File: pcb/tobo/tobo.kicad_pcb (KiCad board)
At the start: 2 copper layers, 57.5 x 61 mm, 88 parts, among them J1 Molex 538-54548-2272, J2 Conn_01x02_Pin, J4 Molex 538-54548-2472, J5 Conn_01x09_Pin, J6 Conn_01x09_Pin, J7 Conn_01x09_Pin, J8 Hroparts Elec TYPE-C-31-M-12, U1 TS5A23167, U10 5015, U11 5015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

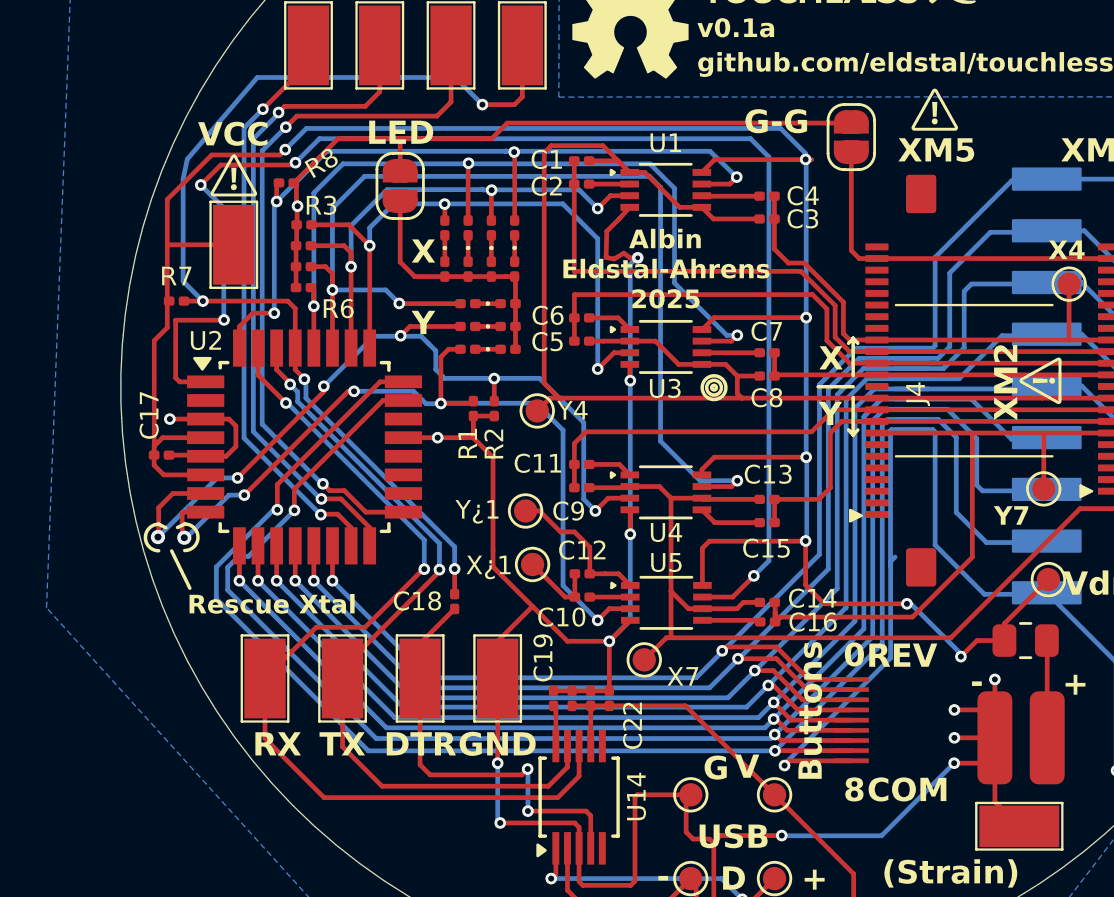
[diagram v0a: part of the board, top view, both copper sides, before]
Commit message: Part numbers selected
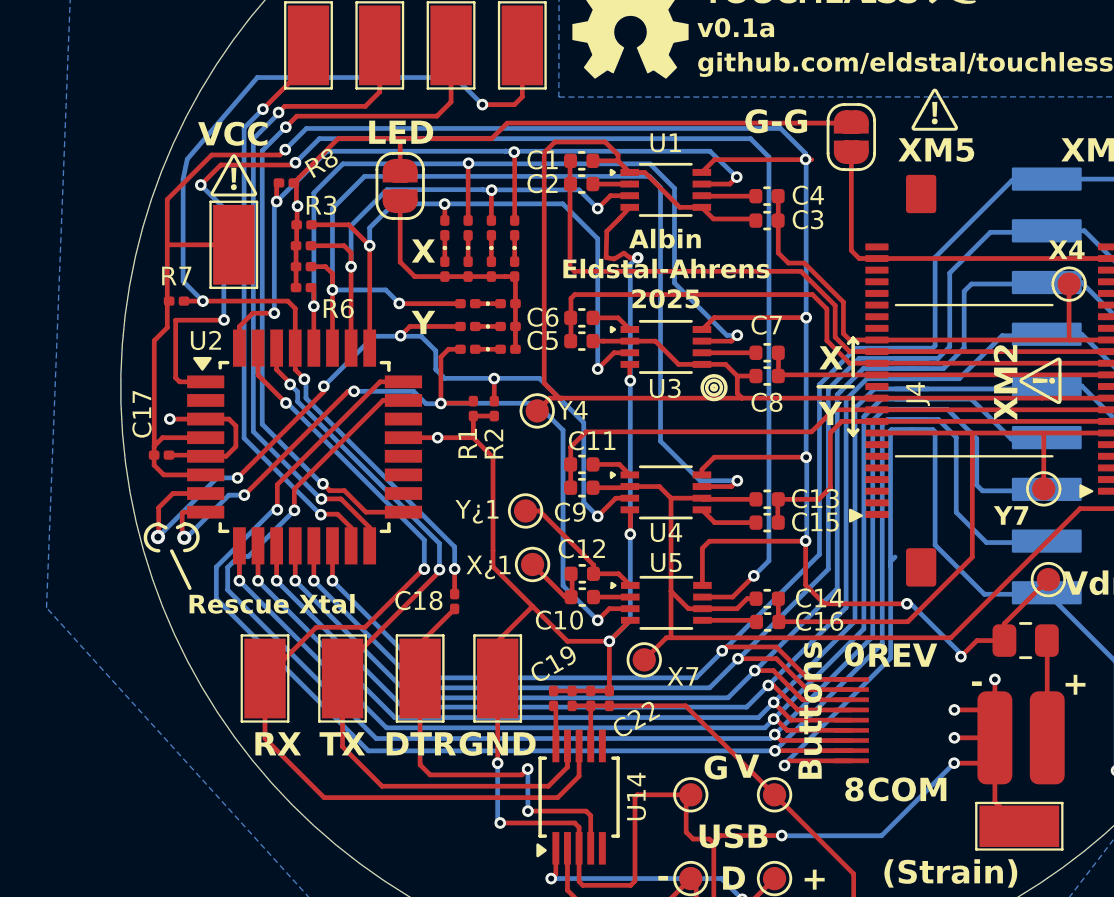
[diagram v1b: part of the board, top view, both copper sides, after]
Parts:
- C1, C10, C11, C12, C13, C14, C15, C16, C2, C3, C4, C5, C6, C7, C8, C9: footprint Capacitor_SMD:C_0201_0603Metric -> Capacitor_SMD:C_0402_1005Metric
- C18: value 100nF -> 0.1uF
- moved C14 0.16 mm to (142.3, 99.1)
- moved C3 0.07 mm to (142.3, 82.8)

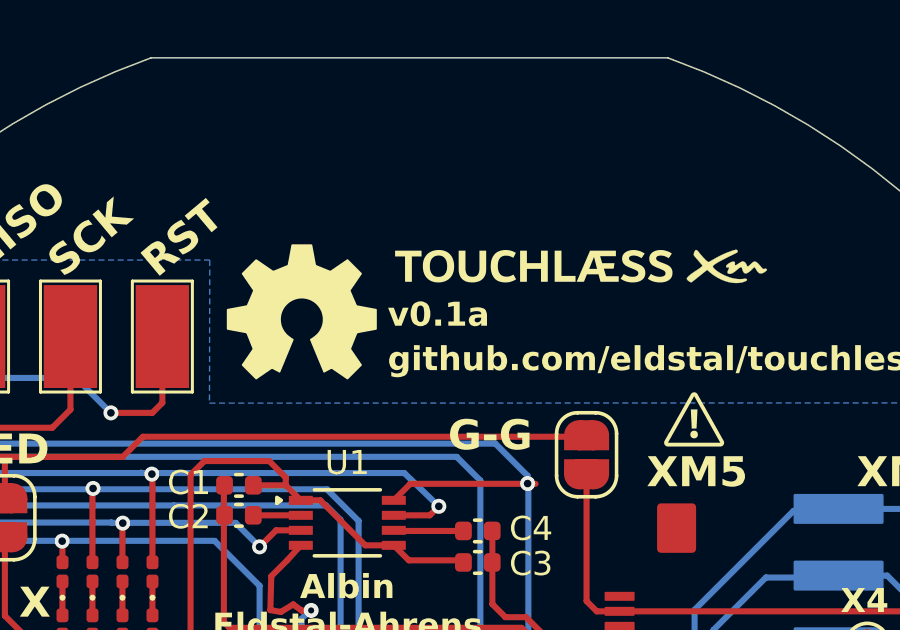
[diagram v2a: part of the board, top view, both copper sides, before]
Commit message: Bumped PCB version to v1.0a
Changes will still be made, I just want it to be labeled
differently from the ones I've ordered for fabrication
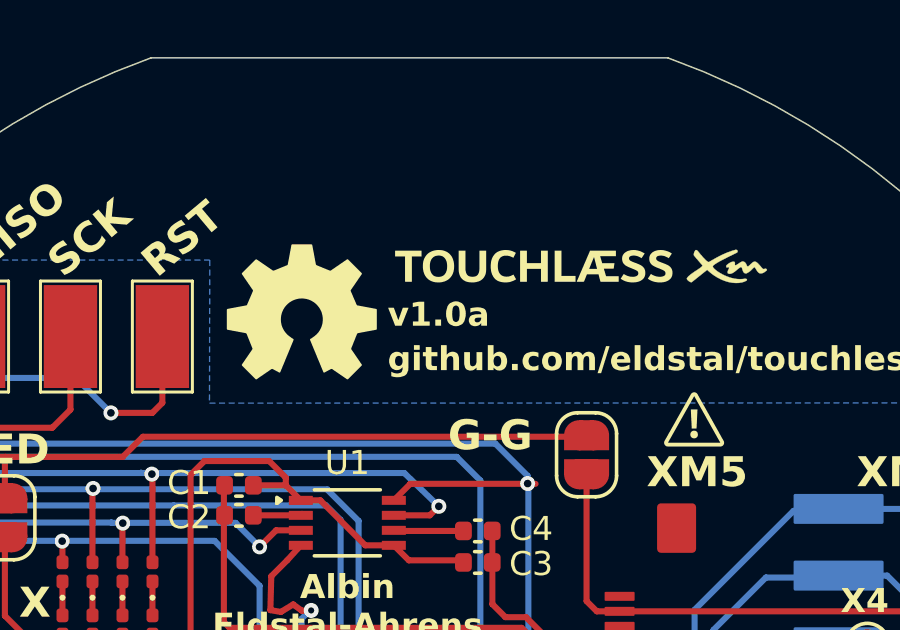
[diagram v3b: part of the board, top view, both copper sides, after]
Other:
- board text added: "v1.0a"
- board text removed: "v0.1a"
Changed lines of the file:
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@@
 		(fp_line
 			(start -2.25 -1.65)
-			(end -2.250001 0.5)
+			(end -2.250002 0.5)
 			(stroke
 				(width 0.1)
@@
 		)
 		(fp_line
-			(start 1.325 -2.099999)
-			(end 1.325 -2.099999)
+			(start 1.325 -2.099998)
+			(end 1.325 -2.099998)
 			(stroke
 				(width 0.2)
@@
 			(start 1.125 -2.1)
 			(mid 1.225001 -2.2)
-			(end 1.325 -2.099999)
+			(end 1.325 -2.099998)
 			(stroke
 				(width 0.2)
@@
 		)
 		(fp_arc
-			(start 1.325 -2.099999)
+			(start 1.325 -2.099998)
 			(mid 1.225 -2.000001)
 			(end 1.125 -2.1)
@@
 		)
 	)
-	(gr_text "v0.1a"
+	(gr_text "v1.0a"
 		(at 139.267504 75.028047 0)
 		(layer "F.SilkS")

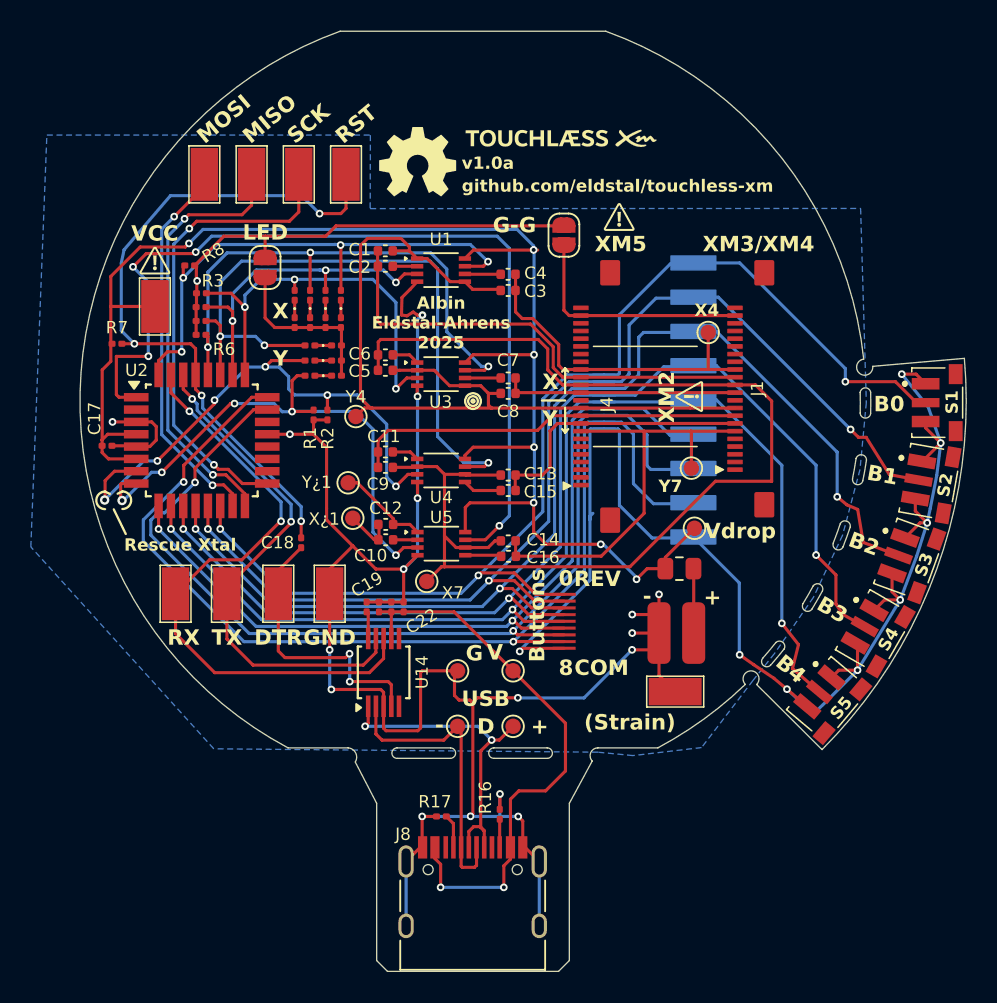
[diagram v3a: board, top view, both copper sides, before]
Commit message: Made the board significantly cheaper to manufacture.
Now there's only one connector (these things are like $5 each :D)
and some of the caps were super expensive too.

Also fixed some incomplete part numbers, so the BOM should be
better for the next attempt at fabrication.
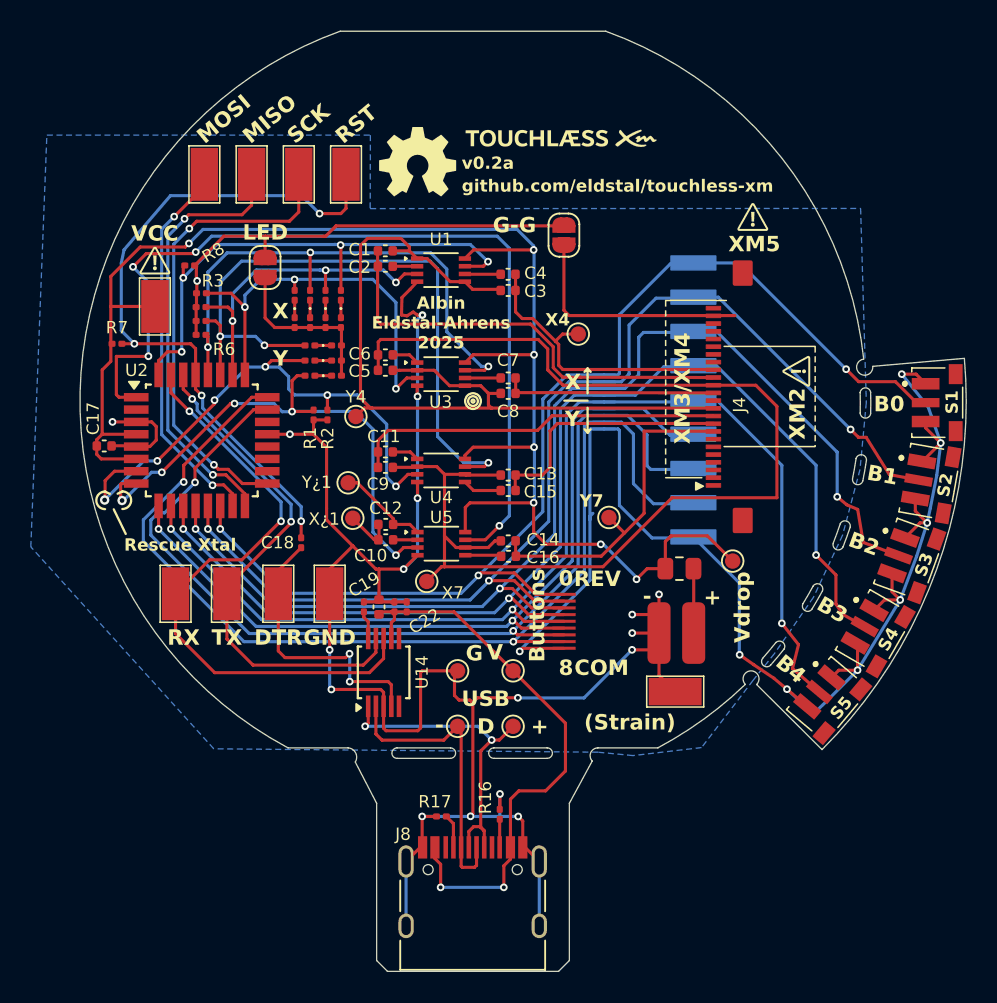
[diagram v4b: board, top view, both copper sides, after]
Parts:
- removed J1: Molex 538-54548-2272, tobo-footprints:molex-545482272
- C17, C20: footprint Capacitor_SMD:C_0201_0603Metric -> Capacitor_SMD:C_0402_1005Metric
- U2: value ATmega328P-A -> ATmega328P-AN
- moved J4 8.60 mm to (156.1, 90.2)
- moved X1 8.43 mm to (146.8, 85.7)
- moved X2 6.23 mm to (148.8, 97.5)
- moved V1 3.27 mm to (156.8, 100.4)
- moved C21 0.20 mm to (134.9, 103.4)
- moved C22 0.20 mm to (135.7, 103.4)
- moved C17 0.19 mm to (116.1, 92.9), turned to 180 degrees
- moved C19 0.18 mm to (132.9, 103.4)
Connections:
- C17 pad 1: +BATT -> GND
- C17 pad 2: GND -> +BATT
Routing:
- net /Y7: track 28.2 -> 21.7 mm
- net +BATT: track 101.2 -> 104.9 mm
- net /X4: track 21.7 -> 19.3 mm
- net /X3: track 30.1 -> 28.7 mm
- net /X1: track 15.4 -> 14.0 mm
- net /Y6: track 18.1 -> 16.7 mm
- net /Y5: track 25.6 -> 24.2 mm
- net /Y4: track 56.9 -> 55.5 mm
- net /X2: track 77.9 -> 79.0 mm
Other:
- board text added: "v0.2a"
- board text removed: "v1.0a"

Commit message: Oops, the connector was on the "safe to cut" board.
It's not a functional issue, just don't go nuts with the saw!
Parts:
- moved J4 4.38 mm to (151.7, 90.2)
- moved V1 0.95 mm to (157.8, 100.1)
- moved X2 0.91 mm to (148.9, 98.5)
- renumbered X7 to X2
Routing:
- net /X2: track 79.0 -> 66.6 mm
- net Net-(J4-GND): track 15.5 -> 9.70 mm
- net /Y7: track 21.7 -> 16.4 mm
- net /Y4: track 55.5 -> 50.7 mm
- net /X1: track 14.0 -> 9.54 mm
- net /Y5: track 24.2 -> 19.8 mm
- net /Y6: track 16.7 -> 12.3 mm
- net /X3: track 28.7 -> 24.4 mm
- net /X4: track 19.3 -> 15.2 mm
- net +BATT: track 104.9 -> 102.9 mm
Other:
- board text added: "v0.3a"
- board text removed: "v0.2a"

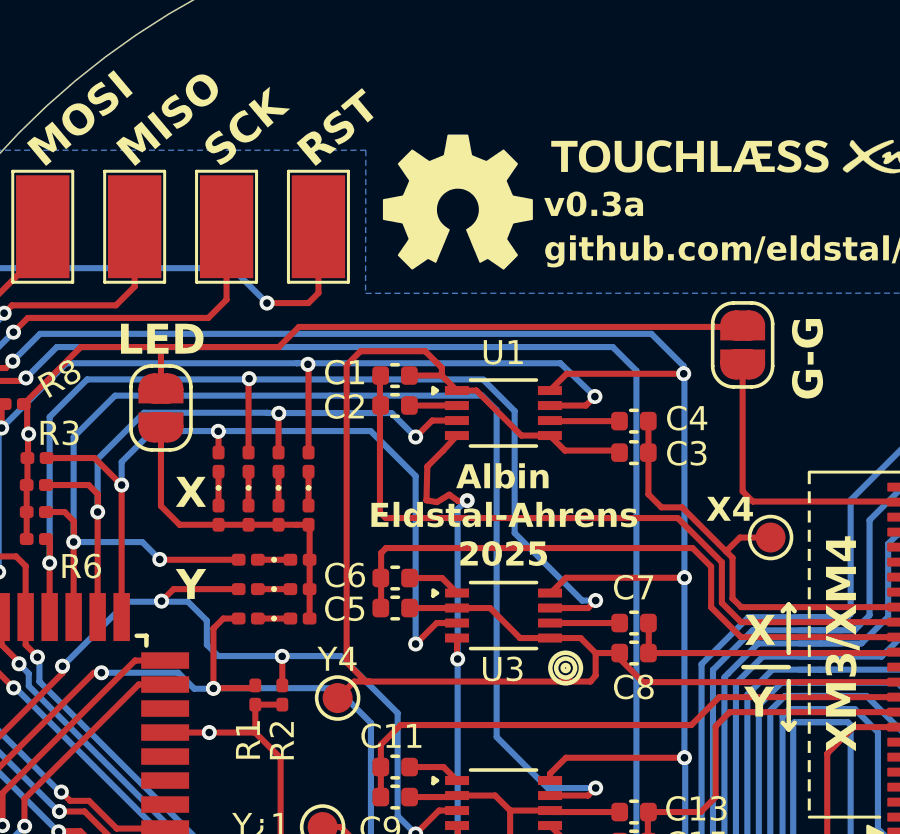
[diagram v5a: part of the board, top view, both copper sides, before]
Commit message: Added clarification to silkscreen
Also bumped PCB version to 0.4
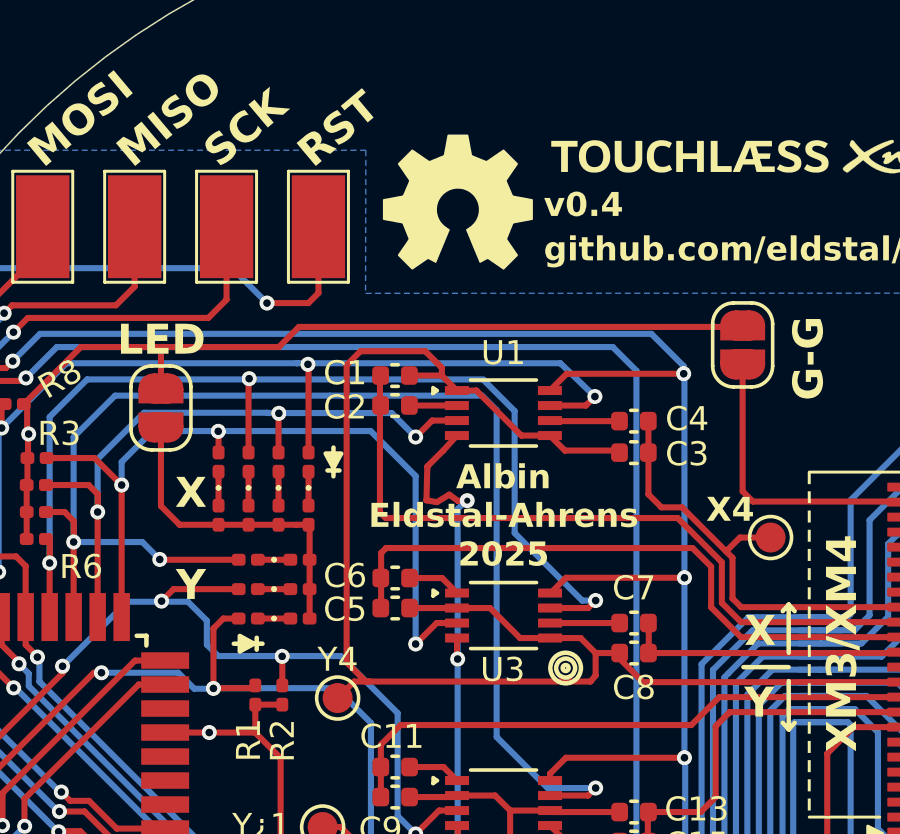
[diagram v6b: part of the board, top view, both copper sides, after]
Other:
- board text added: "v0.4"
- board text removed: "v0.3a"
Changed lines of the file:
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@@
 		(fp_line
 			(start -2.25 -1.65)
-			(end -2.250002 0.5)
+			(end -2.250003 0.5)
 			(stroke
 				(width 0.1)
@@
 		(fp_arc
 			(start 1.325 -2.099998)
-			(mid 1.225 -2.000001)
+			(mid 1.224999 -2)
 			(end 1.125 -2.1)
 			(stroke
@@
 	)
 	(gr_line
+		(start 128.937352 89.189315)
+		(end 129.897354 89.189321)
+		(stroke
+			(width 0.15)
+			(type default)
+		)
+		(layer "F.SilkS")
+	)
+	(gr_line
 		(start 147.435 87.885)
 		(end 147.635 88.105)
@@
 		(layer "F.SilkS")
 	)
+	(gr_line
+		(start 132.26 82.65)
+		(end 132.26 83.61)
+		(stroke
+			(width 0.15)
+			(type default)
+		)
+		(layer "F.SilkS")
+	)
 	(gr_poly
 		(pts
@@
 		(layer "F.SilkS")
 	)
+	(gr_line
+		(start 132.06 83.414998)
+		(end 132.46 83.414998)
+		(stroke
+			(width 0.15)
+			(type default)
+		)
+		(layer "F.SilkS")
+	)
 	(gr_poly
 		(pts
@@
 		(layer "F.SilkS")
 	)
+	(gr_poly
+		(pts
+			(xy 129.612353 89.189321) (xy 129.137357 89.449321) (xy 129.137352 88.929315)
+		)
+		(stroke
+			(width 0.15)
+			(type solid)
+		)
+		(fill solid)
+		(layer "F.SilkS")
+	)
 	(gr_line
 		(start 157.82 86.45)
@@
 	(gr_poly
 		(pts
+			(xy 132.259997 83.324998) (xy 132 82.85) (xy 132.52 82.85)
+		)
+		(stroke
+			(width 0.15)
+			(type solid)
+		)
+		(fill solid)
+		(layer "F.SilkS")
+	)
+	(gr_poly
+		(pts
 			(xy 136.726024 72.216469) (xy 136.727445 72.216574) (xy 136.72886 72.216748) (xy 136.730266 72.216989)
 			(xy 136.73166 72.217294) (xy 136.733041 72.217662) (xy 136.734406 72.218092) (xy 136.735754 72.218581)
@@
 	)
 	(gr_line
+		(start 129.702353 89.38932)
+		(end 129.702355 88.989317)
+		(stroke
+			(width 0.15)
+			(type default)
+		)
+		(layer "F.SilkS")
+	)
+	(gr_line
 		(start 151.911704 92.95)
 		(end 157.82 92.95)
@@
 		)
 	)
-	(gr_text "v0.3a"
+	(gr_text "v0.4"
 		(at 139.267504 75.028047 0)
 		(layer "F.SilkS")
@@
 		)
 	)
+	(group ""
+		(members "0503d321-ba8b-411c-80a6-dedf2bd3afd0" "a17e4008-d070-4823-91b3-d08cb74fb2ae"
+			"e35813a0-bcdf-45fc-87e4-56d5d6b90f51"
+		)
+	)
+	(group ""
+		(members "3d1c75ba-fdd3-4929-aff1-6ed4b638b047" "8f699e78-f5ec-4beb-ad47-1f281a55a1a3"
+			"bb03caa1-7848-48c6-8c09-db7ee058e8f5"
+		)
+	)
